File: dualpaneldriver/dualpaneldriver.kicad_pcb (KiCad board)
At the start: 2 copper layers, 139 parts, among them J201 Conn_01x04, J202 Conn_01x04, J301 LEDPANEL, J401 PIR1, J402 Conn_01x02, J403 PIR2, J404 HALL, J405 PIR3, J406 WS2812CTRL, J407 I2C, J408 CAN, J409 Conn_ARM_JTAG_SWD_10, J410 UART, J411 CAN, J501 LEDPANEL, J601 LEDPANEL, Q201 BSS123, Q202 DMP10H400SK3-13, Q401 AO3400, SW401 POWERON, U201 INA190A2-Q1, U202 SY8502, U203 MCP1754ST-3302E/MB, U301 LM3414HV, U401 STM32F072C8Tx, U402 VEML3328, U403 OPT3001, U404 SN65HVD232, U501 LM3414HV, U601 LM3414HV, Y401 8.000MHz

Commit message: i'm too sleepy to continue
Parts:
- removed C408: 100nF, Capacitor_SMD:C_0603_1608Metric
- removed H102: M3, MountingHole:MountingHole_3.2mm_M3_ISO7380_Pad
- added C413: 100nF, Capacitor_SMD:C_0603_1608Metric, F.Cu at (114.5, 110.8)
- added J412: POWERSW, Connector_PinHeader_2.54mm:PinHeader_1x02_P2.54mm_Vertical, F.Cu at (112.6, 108.2)
- added R420: 1k, Resistor_SMD:R_0603_1608Metric, F.Cu at (116.8, 110.0)
- added R421: 360k, Resistor_SMD:R_0603_1608Metric, F.Cu at (115.3, 108.5)
- added SW402: POWERON, Automated:SW_SPST_PTS636_G, F.Cu at (119.6, 106.3)
- G101: footprint Automated:fully_automated_logo_soldermask -> Automated:falogo_small_copper
- J402: value Conn_01x02 -> USERSW
- SW401: value POWERON -> USER
- moved J202 88.3 mm to (166.5, 75.0), turned to 90 degrees
- moved Q202 84.7 mm to (166.2, 82.5), turned to 90 degrees
- moved D203 84.4 mm to (167.5, 90.0), turned to 0 degrees
- moved R207 80.0 mm to (164.2, 89.0), turned to 180 degrees
- moved R204 79.7 mm to (164.2, 90.5), turned to 0 degrees
- moved Q201 79.0 mm to (164.0, 93.0), turned to 90 degrees
- moved D202 76.5 mm to (159.0, 78.8), turned to 0 degrees
- moved R202 76.4 mm to (160.8, 84.5), turned to 90 degrees
- moved C211 74.9 mm to (161.2, 95.5), turned to 90 degrees
- moved C203 73.5 mm to (133.7, 98.3), turned to 270 degrees
- moved J201 73.4 mm to (155.0, 75.0), turned to 90 degrees
- moved R201 73.4 mm to (158.0, 82.8), turned to 270 degrees
- moved C204 73.2 mm to (159.8, 91.8), turned to 270 degrees
- moved C212 72.7 mm to (159.8, 95.5), turned to 90 degrees
- moved R210 72.6 mm to (136.6, 98.3), turned to 90 degrees
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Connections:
- U401 pad 19: /Microcontroller/ADC_IN9 -> /Microcontroller/WAKEUP_SW
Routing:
- net GNDD: track 0.00 -> 198.7 mm
- net +3V3: track 0.00 -> 127.0 mm
- net +5VL: track 0.00 -> 89.3 mm
- net GND: track 68.0 -> 157.0 mm
- net +48V: track 72.2 -> 143.6 mm
- net VBUS: track 0.00 -> 55.9 mm, vias 0 -> 2
- net /Microcontroller/nRST: track 0.00 -> 46.3 mm, vias 0 -> 2
- net /Microcontroller/WAKEUP_SW: track 0.00 -> 39.1 mm, vias 0 -> 4
- net Net-(J401-Pad2): track 0.00 -> 38.9 mm, vias 0 -> 2
- net /Microcontroller/CAND_P: track 0.00 -> 35.6 mm
- net /Microcontroller/CAND_N: track 0.00 -> 34.5 mm
- net /Microcontroller/I2S1_SD: track 0.00 -> 33.4 mm
- net Net-(J403-Pad2): track 0.00 -> 21.0 mm, vias 0 -> 2
- net GNDA: track 0.00 -> 17.7 mm
- net /Power Supply/SUP_GND: track 0.00 -> 14.3 mm
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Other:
- board outline added: 90 x 40 mm
- net class Default: clearance 0.1524 -> 0.2
- rule trace_clearance: 0.1524 -> 0.2

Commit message: 100% routed, silkscreen still fucked up
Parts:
- G102: moved to B.Cu
- J401: value PIR1 -> PIR3
- J405: value PIR3 -> PIR1
- moved G102 76.6 mm to (126.5, 106.6), turned to 90 degrees
- moved NT401 17.3 mm to (130.7, 99.9), turned to 180 degrees
- moved R406 17.2 mm to (138.6, 88.6), turned to 180 degrees
- moved R413 6.77 mm to (122.0, 93.4), turned to 0 degrees
- moved R414 3.63 mm to (158.6, 109.2)
- moved R410 2.46 mm to (142.0, 99.0)
- moved G101 0.91 mm to (127.1, 106.7)
- moved R211 0.41 mm to (139.4, 97.3)
- turned R403 to 270 degrees
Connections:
- R406 pad 2: /Microcontroller/MOTION1 -> /Microcontroller/MOTION3
- R413 pad 2: /Microcontroller/MOTION3 -> /Microcontroller/MOTION1
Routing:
- net +3V3: track 127.0 -> 285.7 mm, vias 0 -> 8
- net /LED Driver 1/DIM: track 4.03 -> 160.6 mm, vias 0 -> 6
- net /LED Driver 2/DIM: track 4.03 -> 102.4 mm, vias 0 -> 8
- net /Microcontroller/LED1: track 0.00 -> 86.6 mm, vias 0 -> 4
- net ADCIN_CSA: track 0.00 -> 84.6 mm, vias 0 -> 6
- net /Microcontroller/DAC1: track 0.00 -> 80.6 mm, vias 0 -> 4
- net 48V_EN: track 0.00 -> 64.7 mm, vias 0 -> 4
- net /LED Driver 3/DIM: track 4.03 -> 68.5 mm, vias 0 -> 6
- net /Microcontroller/LED2: track 0.00 -> 62.3 mm, vias 0 -> 6
- net /Microcontroller/LED3: track 0.00 -> 58.2 mm, vias 0 -> 2
- net /Microcontroller/DAC2: track 11.2 -> 66.5 mm, vias 0 -> 6
- net /Microcontroller/HALL1: track 0.00 -> 51.3 mm, vias 0 -> 4
- net +5VL: track 89.3 -> 127.2 mm, vias 0 -> 5
- net GNDA: track 17.7 -> 54.0 mm, vias 0 -> 4
- net VDDA: track 6.15 -> 41.9 mm, vias 0 -> 4
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- added copper zone on B.Cu, net GND
- added copper zone on F.Cu, net GND
- added copper zone on B.Cu, net GNDD
- added copper zone on F.Cu, net GNDD

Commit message: I think it is done!?!
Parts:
- moved G102 15.4 mm to (129.2, 91.4), turned to 180 degrees
- moved G101 1.36 mm to (126.7, 108.0), turned to 90 degrees
- moved H101 0.47 mm to (170.2, 99.4)
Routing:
- net GNDD: track 187.7 -> 195.4 mm, vias 24 -> 68
- net +5VL: track 127.2 -> 130.8 mm
- net /Microcontroller/HALL1: track 51.3 -> 54.8 mm
- net /LED Driver 3/DIM: track 68.5 -> 71.5 mm
- net /Microcontroller/LED2: track 62.3 -> 65.2 mm
- net /Microcontroller/DAC1: track 80.6 -> 83.0 mm
- net +3V3: track 285.7 -> 287.9 mm
- net /Microcontroller/OPT_IRQ: track 38.5 -> 39.9 mm
- net /Microcontroller/WAKEUP_SW: track 39.4 -> 40.6 mm
- net /Microcontroller/BOOT0: track 23.7 -> 24.8 mm
- net +48V: track 143.6 -> 144.6 mm
- net Net-(J403-Pad2): track 27.2 -> 28.1 mm
- net /LED Driver 1/DIM: track 160.6 -> 161.4 mm
- net /Microcontroller/I2C_SDA: track 28.0 -> 28.7 mm
- net /Microcontroller/DAC2: track 66.5 -> 67.2 mm
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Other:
- net class Default: clearance 0.2 -> 0.16
- rule pad_to_mask_clearance: 0.051 -> 0.04
- rule solder_mask_min_width: 0.25 -> 0.1
- rule trace_clearance: 0.2 -> 0.16
- board text added: ""POWER""
- board text added: ""USER""
- board text added: "+ -"
- board text added: "+ 1"
- board text added: "+ 2"
- board text added: "+ 3"
- board text added: "++"
- board text added: "+3.3V U1TX U1RX GNDD"
- board text added: "+5V CANH CANL GNDD"
- board text added: "+5V SIG GND"
- board text added: "--"
- board text added: "1"
- board text added: "1.0"
- board text added: "2"
- board text added: "3"
- board text added: "3 2 1"
- board text added: "3.3V"
- board text added: "3V3 SCL SDA GNDD"
- board text added: "3V3 SIG GNDD"
- board text added: "5"
- board text added: "6"
- board text added: "7"
- board text added: "9"
- board text added: "ACT1"
- board text added: "CAN"
- board text added: "CANesys"
- board text added: "CANesys 1.0"
- board text added: "D:"
- board text added: "ERR"
- board text added: "Fully Automated OÜ"
- board text added: "G CANL-H 5V"
- board text added: "G R T 3V3"
- board text added: "GND"
- board text added: "GND SIG +5V"
- board text added: "GNDD SIG 3V3"
- board text added: "GNDD nPOWER_ON"
- board text added: "GNDD nUSER"
- board text added: "HALL"
- board text added: "I'm naked!!!"
- board text added: "I2C"
- board text added: "IN"
- board text added: "JLCJLCJLCJLC"
- board text added: "MADE IN ANGER"
- board text added: "OUT"
- board text added: "PIR1"
- board text added: "PIR2"
- board text added: "PIR3"
- board text added: "SW"
- board text added: "Triple Channel Constant Current Buck Mode LED Controller with CAN interface"
- board text added: "UART"
- board text added: "VBUS"
- board text added: "WS2812"
- board text added: "WSLED"
- board text added: "automated.ee"
- board text added: "don't look"
- board text added: "in"
- board text added: "max 5 A"
- board text added: "max 60 V"
- board text added: "out"
- board text added: "symbol by @mxsparks@vulpine.club"

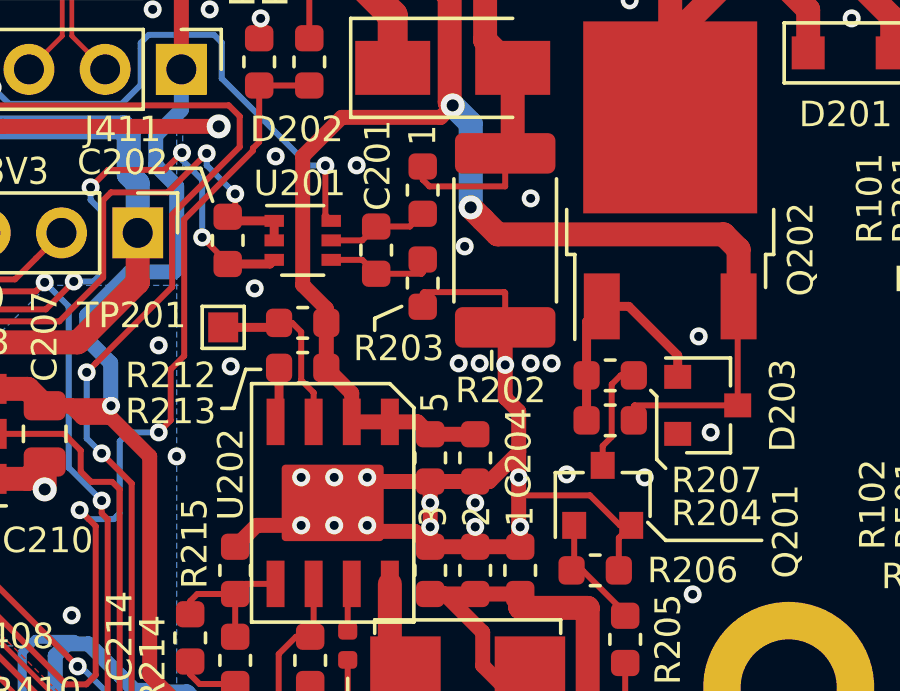
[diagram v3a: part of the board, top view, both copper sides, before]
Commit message: changed input cap on the LED driver's DCDC
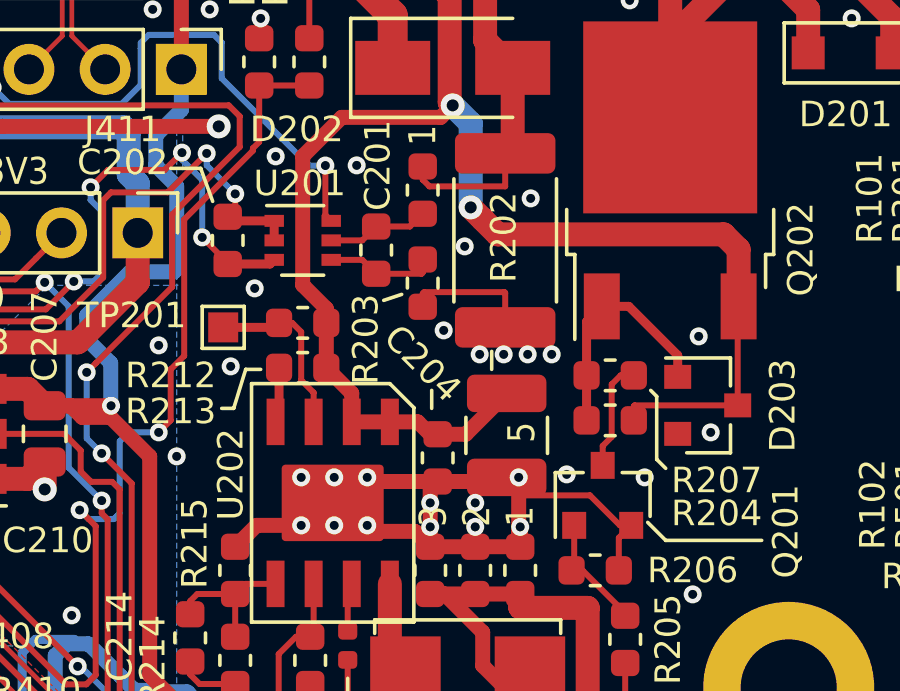
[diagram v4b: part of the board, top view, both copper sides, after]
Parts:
- C205: footprint Capacitor_SMD:C_0603_1608Metric -> Capacitor_SMD:C_1210_3225Metric
- moved C205 2.66 mm to (160.8, 91.0)
- moved C204 1.25 mm to (158.5, 91.8)
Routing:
- net GND: track 168.3 -> 161.0 mm
- net VBUS: track 57.6 -> 59.3 mm
